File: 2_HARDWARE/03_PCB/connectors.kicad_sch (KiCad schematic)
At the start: 19 parts, among them J1 TYPE-C-31-M-12, J2 SMA, J3 SMA, J4 BNC, J5 PH-00244

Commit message: MINOR: Changed board outline and started component placement.
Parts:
- H1: footprint MountingHole:MountingHole_3.2mm_M3_Pad -> MountingHole:MountingHole_3.2mm_M3_Pad_TopBottom
- H2, H3, H4: footprint MountingHole:MountingHole_3.2mm_M3_Pad -> MountingHole:MountingHole_3.2mm_M3_Pad_Via
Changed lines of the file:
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@@
 			)
 		)
-		(property "Footprint" "MountingHole:MountingHole_3.2mm_M3_Pad"
+		(property "Footprint" "MountingHole:MountingHole_3.2mm_M3_Pad_Via"
 			(at 242.57 17.78 0)
 			(effects
@@
 	)
 	(symbol
+		(lib_name "MountingHole_Pad_1")
 		(lib_id "Mechanical:MountingHole_Pad")
 		(at 232.41 17.78 0)
@@
 			)
 		)
-		(property "Footprint" "MountingHole:MountingHole_3.2mm_M3_Pad"
+		(property "Footprint" "MountingHole:MountingHole_3.2mm_M3_Pad_TopBottom"
 			(at 232.41 17.78 0)
 			(effects
@@
 			)
 		)
-		(property "Footprint" "MountingHole:MountingHole_3.2mm_M3_Pad"
+		(property "Footprint" "MountingHole:MountingHole_3.2mm_M3_Pad_Via"
 			(at 251.46 17.78 0)
 			(effects
@@
 			)
 		)
-		(property "Footprint" "MountingHole:MountingHole_3.2mm_M3_Pad"
+		(property "Footprint" "MountingHole:MountingHole_3.2mm_M3_Pad_Via"
 			(at 260.35 17.78 0)
 			(effects

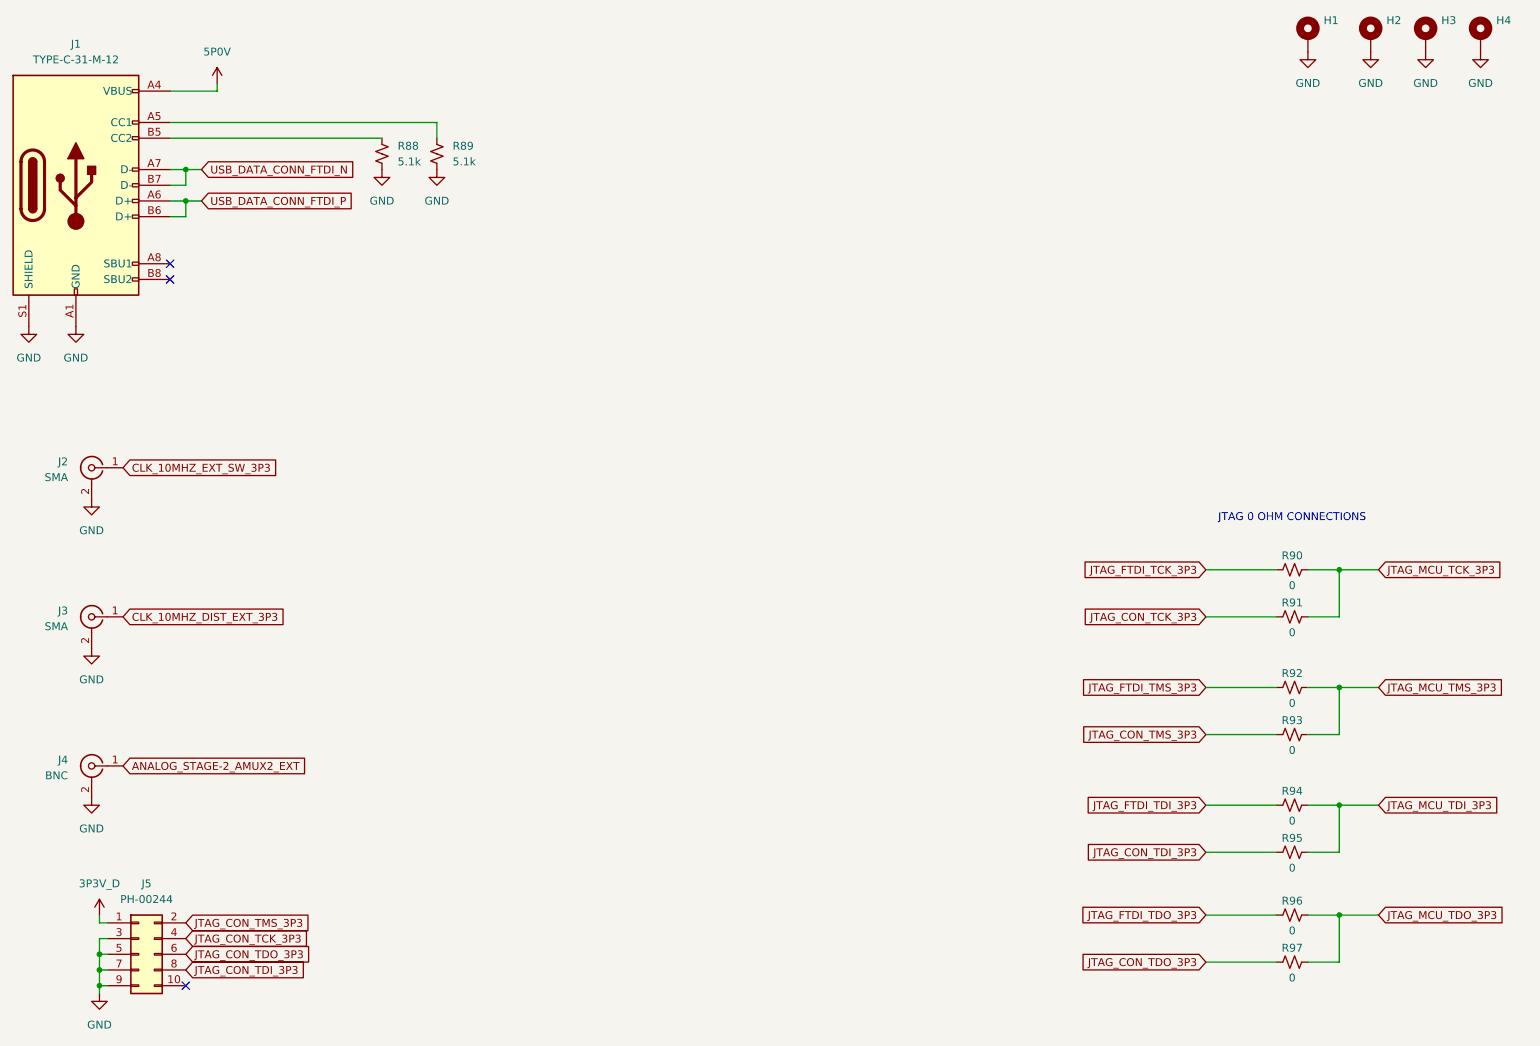
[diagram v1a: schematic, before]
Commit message: MINOR: Changed Boot Select Switches to Pull-Downs / Pull Up DNI and continued layout.
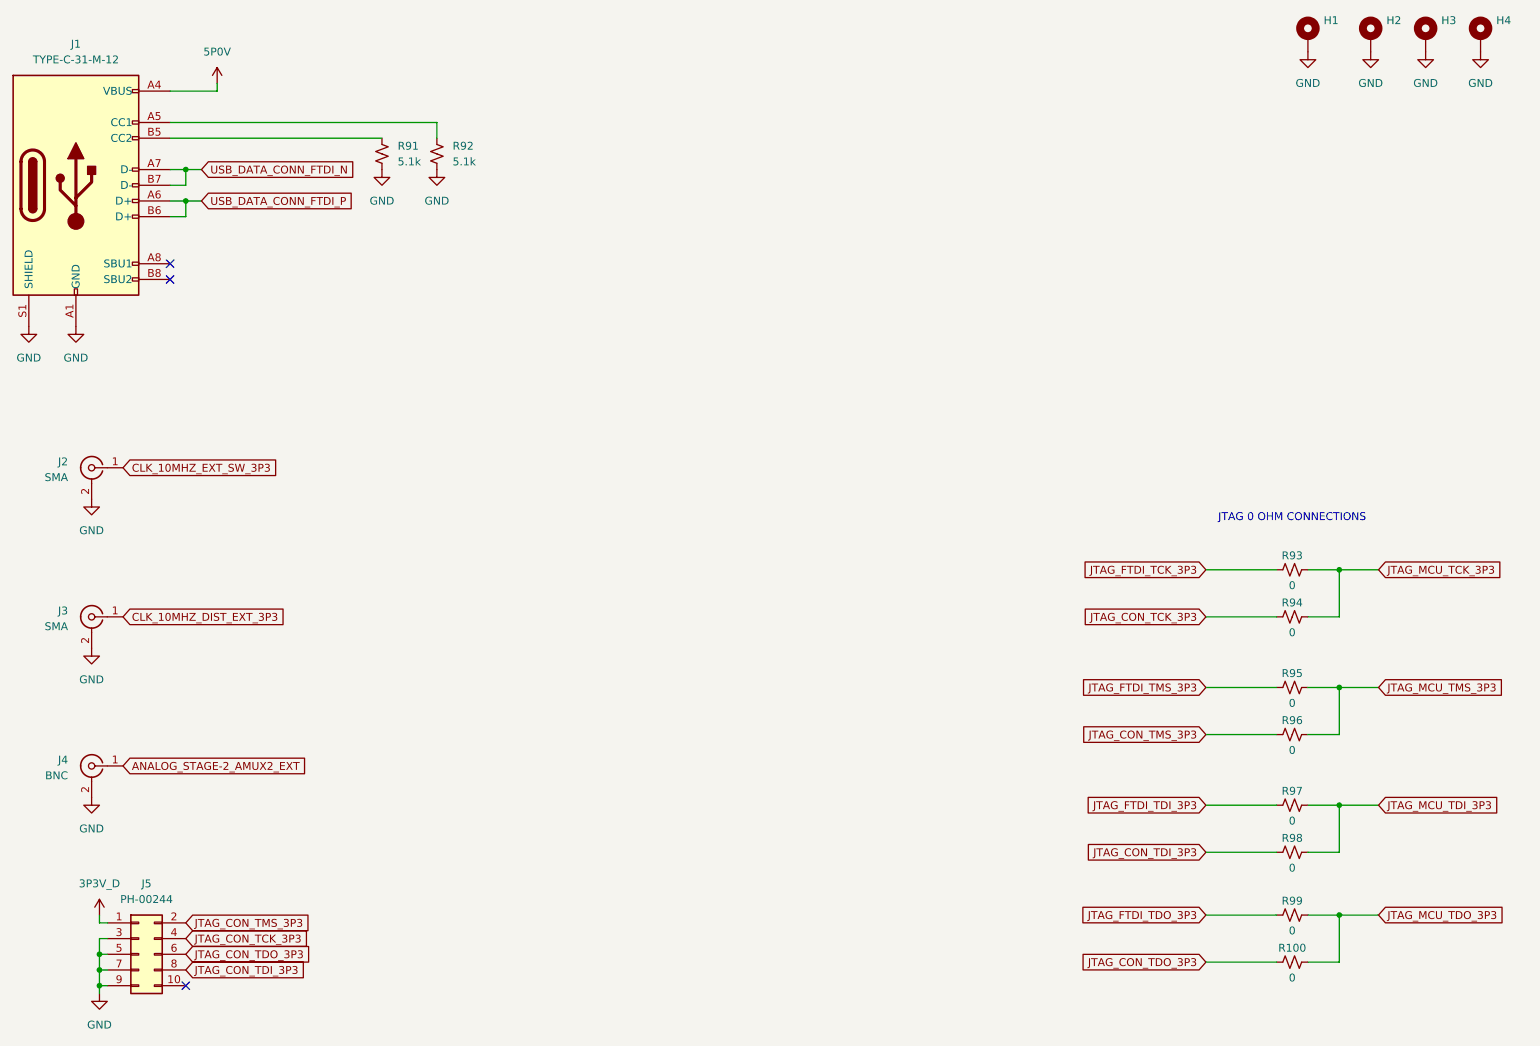
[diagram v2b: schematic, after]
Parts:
- renumbered R97 to R100, R88 to R91, R89 to R92, R90 to R93, R91 to R94, R92 to R95, R93 to R96, R94 to R97, R95 to R98, R96 to R99
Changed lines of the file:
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@@
 		(on_board yes)
 		(dnp no)
-		(property "Reference" "R97"
+		(property "Reference" "R100"
 			(at 229.87 165.354 90)
 			(effects
@@
 			(project "arb"
 				(path "/866ef9be-3b01-4288-a6e0-a2357aa17e50/eb105004-087f-4ea7-8291-809b214299af"
-					(reference "R97")
+					(reference "R100")
 					(unit 1)
 				)
@@
 		(dnp no)
 		(fields_autoplaced yes)
-		(property "Reference" "#PWR0299"
+		(property "Reference" "#PWR0295"
 			(at 35.56 147.32 0)
 			(effects
@@
 			(project "arb"
 				(path "/866ef9be-3b01-4288-a6e0-a2357aa17e50/eb105004-087f-4ea7-8291-809b214299af"
-					(reference "#PWR0299")
+					(reference "#PWR0295")
 					(unit 1)
 				)
@@
 		(dnp no)
 		(fields_autoplaced yes)
-		(property "Reference" "#PWR0300"
+		(property "Reference" "#PWR0296"
 			(at 36.83 163.83 0)
 			(effects
@@
 			(project "arb"
 				(path "/866ef9be-3b01-4288-a6e0-a2357aa17e50/eb105004-087f-4ea7-8291-809b214299af"
-					(reference "#PWR0300")
+					(reference "#PWR0296")
 					(unit 1)
 				)
@@
 		(on_board yes)
 		(dnp no)
-		(property "Reference" "R92"
+		(property "Reference" "R95"
 			(at 229.87 120.904 90)
 			(effects
@@
 			(project "arb"
 				(path "/866ef9be-3b01-4288-a6e0-a2357aa17e50/eb105004-087f-4ea7-8291-809b214299af"
-					(reference "R92")
+					(reference "R95")
 					(unit 1)
 				)
@@
 		(dnp no)
 		(fields_autoplaced yes)
-		(property "Reference" "#PWR0307"
+		(property "Reference" "#PWR0303"
 			(at 251.46 26.67 0)
 			(effects
@@
 			(project "arb"
 				(path "/866ef9be-3b01-4288-a6e0-a2357aa17e50/eb105004-087f-4ea7-8291-809b214299af"
-					(reference "#PWR0307")
+					(reference "#PWR0303")
 					(unit 1)
 				)
@@
 		(dnp no)
 		(fields_autoplaced yes)
-		(property "Reference" "R89"
+		(property "Reference" "R92"
 			(at 93.98 35.5599 0)
 			(effects
@@
 			(project "arb"
 				(path "/866ef9be-3b01-4288-a6e0-a2357aa17e50/eb105004-087f-4ea7-8291-809b214299af"
-					(reference "R89")
+					(reference "R92")
 					(unit 1)
 				)
@@
 		(dnp no)
 		(fields_autoplaced yes)
-		(property "Reference" "#PWR0295"
+		(property "Reference" "#PWR0291"
 			(at 25.4 71.12 0)
 			(effects
@@
 			(project "arb"
 				(path "/866ef9be-3b01-4288-a6e0-a2357aa17e50/eb105004-087f-4ea7-8291-809b214299af"
-					(reference "#PWR0295")
+					(reference "#PWR0291")
 					(unit 1)
 				)
@@
 		(dnp no)
 		(fields_autoplaced yes)
-		(property "Reference" "#PWR0303"
+		(property "Reference" "#PWR0299"
 			(at 82.55 45.72 0)
 			(effects
@@
 			(project "arb"
 				(path "/866ef9be-3b01-4288-a6e0-a2357aa17e50/eb105004-087f-4ea7-8291-809b214299af"
-					(reference "#PWR0303")
+					(reference "#PWR0299")
 					(unit 1)
 				)
@@
 		(dnp no)
 		(fields_autoplaced yes)
-		(property "Reference" "#PWR0297"
+		(property "Reference" "#PWR0293"
 			(at 35.56 99.06 0)
 			(effects
@@
 			(project "arb"
 				(path "/866ef9be-3b01-4288-a6e0-a2357aa17e50/eb105004-087f-4ea7-8291-809b214299af"
-					(reference "#PWR0297")
+					(reference "#PWR0293")
 					(unit 1)
 				)
@@
 		(dnp no)
 		(fields_autoplaced yes)
-		(property "Reference" "#PWR0298"
+		(property "Reference" "#PWR0294"
 			(at 35.56 123.19 0)
 			(effects
@@
 			(project "arb"
 				(path "/866ef9be-3b01-4288-a6e0-a2357aa17e50/eb105004-087f-4ea7-8291-809b214299af"
-					(reference "#PWR0298")
+					(reference "#PWR0294")
 					(unit 1)
 				)
@@
 		(dnp no)
 		(fields_autoplaced yes)
-		(property "Reference" "#PWR0308"
+		(property "Reference" "#PWR0304"
 			(at 260.35 26.67 0)
 			(effects
@@
 			(project "arb"
 				(path "/866ef9be-3b01-4288-a6e0-a2357aa17e50/eb105004-087f-4ea7-8291-809b214299af"
-					(reference "#PWR0308")
+					(reference "#PWR0304")
 					(unit 1)
 				)
@@
 		(dnp no)
 		(fields_autoplaced yes)
-		(property "Reference" "#PWR0306"
+		(property "Reference" "#PWR0302"
 			(at 242.57 26.67 0)
 			(effects
@@
 			(project "arb"
 				(path "/866ef9be-3b01-4288-a6e0-a2357aa17e50/eb105004-087f-4ea7-8291-809b214299af"
-					(reference "#PWR0306")
+					(reference "#PWR0302")
 					(unit 1)
 				)
@@
 		(dnp no)
 		(fields_autoplaced yes)
-		(property "Reference" "#PWR0301"
+		(property "Reference" "#PWR0297"
 			(at 36.83 179.07 0)
 			(effects
@@
 			(project "arb"
 				(path "/866ef9be-3b01-4288-a6e0-a2357aa17e50/eb105004-087f-4ea7-8291-809b214299af"
-					(reference "#PWR0301")
+					(reference "#PWR0297")
 					(unit 1)
 				)
@@
 		(dnp no)
 		(fields_autoplaced yes)
-		(property "Reference" "#PWR0304"
+		(property "Reference" "#PWR0300"
 			(at 91.44 45.72 0)
 			(effects
@@
 			(project "arb"
 				(path "/866ef9be-3b01-4288-a6e0-a2357aa17e50/eb105004-087f-4ea7-8291-809b214299af"
-					(reference "#PWR0304")
+					(reference "#PWR0300")
 					(unit 1)
 				)
@@
 		(on_board yes)
 		(dnp no)
-		(property "Reference" "R91"
+		(property "Reference" "R94"
 			(at 229.87 109.474 90)
 			(effects
@@
 			(project "arb"
 				(path "/866ef9be-3b01-4288-a6e0-a2357aa17e50/eb105004-087f-4ea7-8291-809b214299af"
-					(reference "R91")
+					(reference "R94")
 					(unit 1)
 				)
@@
 		(on_board yes)
 		(dnp no)
-		(property "Reference" "R94"
+		(property "Reference" "R97"
 			(at 229.87 139.954 90)
 			(effects
@@
 			(project "arb"
 				(path "/866ef9be-3b01-4288-a6e0-a2357aa17e50/eb105004-087f-4ea7-8291-809b214299af"
-					(reference "R94")
+					(reference "R97")
 					(unit 1)
 				)
@@
 		(dnp no)
 		(fields_autoplaced yes)
-		(property "Reference" "#PWR0296"
+		(property "Reference" "#PWR0292"
 			(at 33.02 71.12 0)
 			(effects
@@
 			(project "arb"
 				(path "/866ef9be-3b01-4288-a6e0-a2357aa17e50/eb105004-087f-4ea7-8291-809b214299af"
-					(reference "#PWR0296")
+					(reference "#PWR0292")
 					(unit 1)
 				)
@@
 		(on_board yes)
 		(dnp no)
-		(property "Reference" "R95"
+		(property "Reference" "R98"
 			(at 229.87 147.574 90)
 			(effects
@@
 			(project "arb"
 				(path "/866ef9be-3b01-4288-a6e0-a2357aa17e50/eb105004-087f-4ea7-8291-809b214299af"
-					(reference "R95")
+					(reference "R98")
 					(unit 1)
 				)
@@
 		(on_board yes)
 		(dnp no)
-		(property "Reference" "R96"
+		(property "Reference" "R99"
 			(at 229.87 157.734 90)
 			(effects
@@
 			(project "arb"
 				(path "/866ef9be-3b01-4288-a6e0-a2357aa17e50/eb105004-087f-4ea7-8291-809b214299af"
-					(reference "R96")
+					(reference "R99")
 					(unit 1)
 				)
@@
 		(on_board yes)
 		(dnp no)
-		(property "Reference" "R90"
+		(property "Reference" "R93"
 			(at 229.87 101.854 90)
 			(effects
@@
 			(project "arb"
 				(path "/866ef9be-3b01-4288-a6e0-a2357aa17e50/eb105004-087f-4ea7-8291-809b214299af"
-					(reference "R90")
+					(reference "R93")
 					(unit 1)
 				)
@@
 		(dnp no)
 		(fields_autoplaced yes)
-		(property "Reference" "#PWR0302"
+		(property "Reference" "#PWR0298"
 			(at 55.88 29.21 0)
 			(effects
@@
 			(project "arb"
 				(path "/866ef9be-3b01-4288-a6e0-a2357aa17e50/eb105004-087f-4ea7-8291-809b214299af"
-					(reference "#PWR0302")
+					(reference "#PWR0298")
 					(unit 1)
 				)
@@
 		(dnp no)
 		(fields_autoplaced yes)
-		(property "Reference" "R88"
+		(property "Reference" "R91"
 			(at 85.09 35.5599 0)
 			(effects
@@
 			(project "arb"
 				(path "/866ef9be-3b01-4288-a6e0-a2357aa17e50/eb105004-087f-4ea7-8291-809b214299af"
-					(reference "R88")
+					(reference "R91")
 					(unit 1)
 				)
@@
 		(dnp no)
 		(fields_autoplaced yes)
-		(property "Reference" "#PWR0305"
+		(property "Reference" "#PWR0301"
 			(at 232.41 26.67 0)
 			(effects
@@
 			(project "arb"
 				(path "/866ef9be-3b01-4288-a6e0-a2357aa17e50/eb105004-087f-4ea7-8291-809b214299af"
-					(reference "#PWR0305")
+					(reference "#PWR0301")
 					(unit 1)
 				)
@@
 		(on_board yes)
 		(dnp no)
-		(property "Reference" "R93"
+		(property "Reference" "R96"
 			(at 229.87 128.524 90)
 			(effects
@@
 			(project "arb"
 				(path "/866ef9be-3b01-4288-a6e0-a2357aa17e50/eb105004-087f-4ea7-8291-809b214299af"
-					(reference "R93")
-					(unit 1)
-				)
+					(reference "R96")
+					(unit 1)
+				)

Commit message: FEAT: Routed Analog and all Misc Signals. Routing is complete.
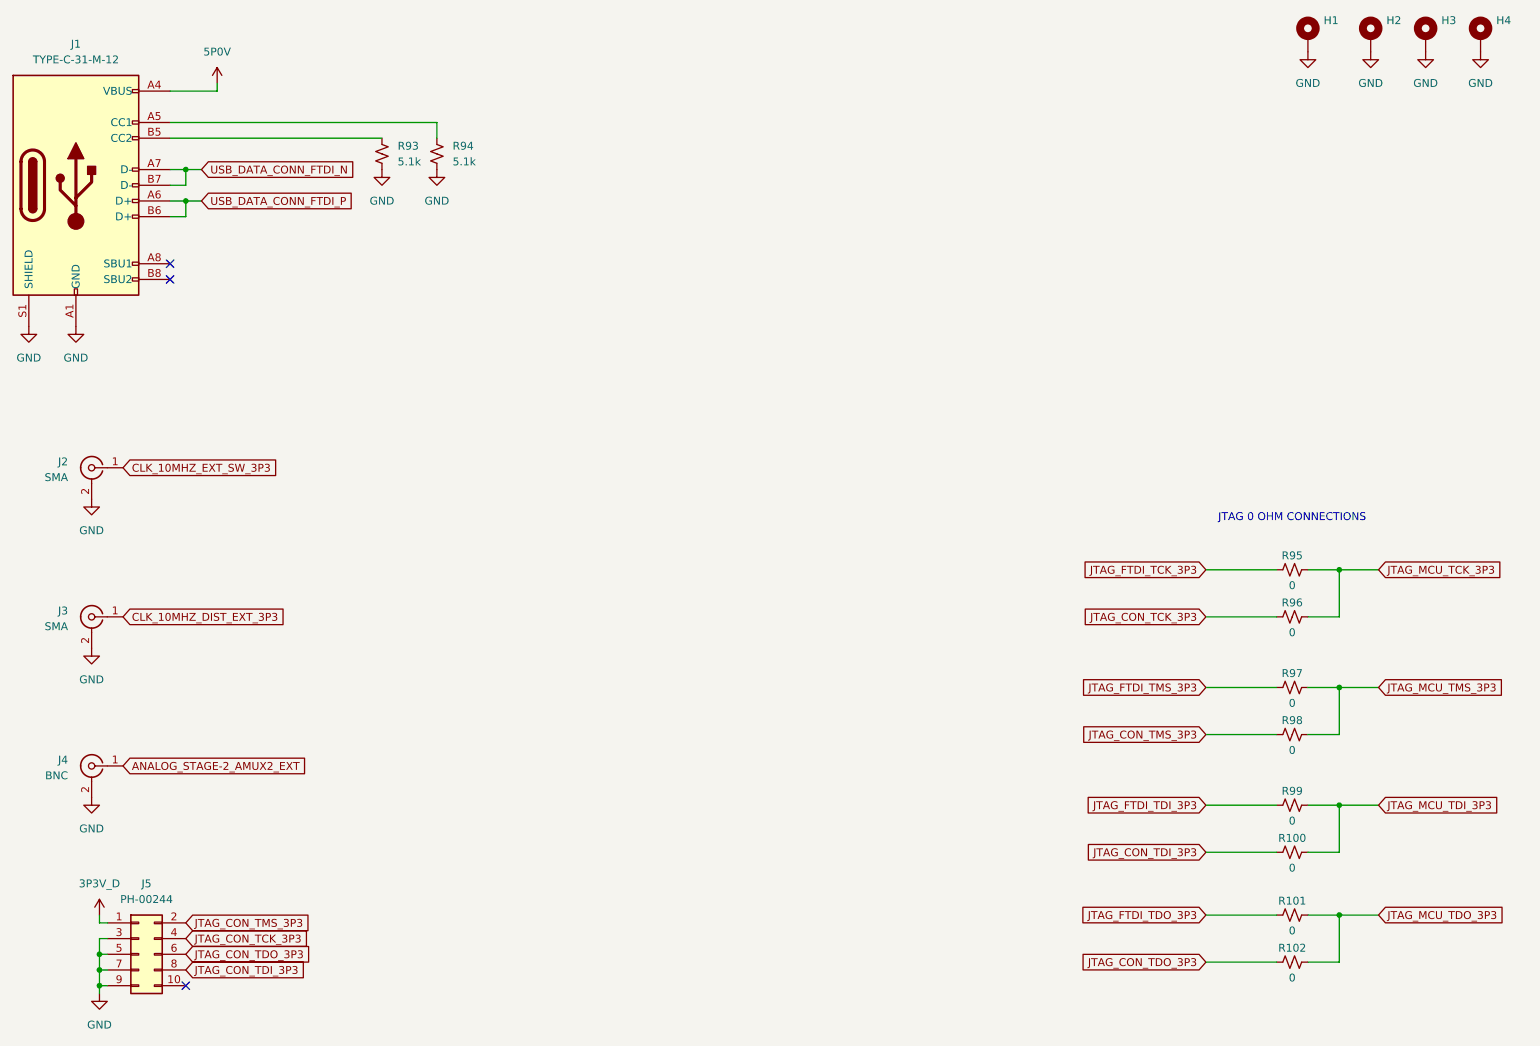
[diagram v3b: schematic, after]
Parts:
- renumbered R98 to R100, R99 to R101, R100 to R102, R91 to R93, R92 to R94, R93 to R95, R94 to R96, R95 to R97, R96 to R98, R97 to R99
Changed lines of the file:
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@@
 		(on_board yes)
 		(dnp no)
-		(property "Reference" "R100"
+		(property "Reference" "R102"
 			(at 229.87 165.354 90)
 			(effects
@@
 			(project "arb"
 				(path "/866ef9be-3b01-4288-a6e0-a2357aa17e50/eb105004-087f-4ea7-8291-809b214299af"
-					(reference "R100")
+					(reference "R102")
 					(unit 1)
 				)
@@
 		(on_board yes)
 		(dnp no)
-		(property "Reference" "R95"
+		(property "Reference" "R97"
 			(at 229.87 120.904 90)
 			(effects
@@
 			(project "arb"
 				(path "/866ef9be-3b01-4288-a6e0-a2357aa17e50/eb105004-087f-4ea7-8291-809b214299af"
-					(reference "R95")
+					(reference "R97")
 					(unit 1)
 				)
@@
 		(dnp no)
 		(fields_autoplaced yes)
-		(property "Reference" "R92"
+		(property "Reference" "R94"
 			(at 93.98 35.5599 0)
 			(effects
@@
 			(project "arb"
 				(path "/866ef9be-3b01-4288-a6e0-a2357aa17e50/eb105004-087f-4ea7-8291-809b214299af"
-					(reference "R92")
+					(reference "R94")
 					(unit 1)
 				)
@@
 		(on_board yes)
 		(dnp no)
-		(property "Reference" "R94"
+		(property "Reference" "R96"
 			(at 229.87 109.474 90)
 			(effects
@@
 			(project "arb"
 				(path "/866ef9be-3b01-4288-a6e0-a2357aa17e50/eb105004-087f-4ea7-8291-809b214299af"
-					(reference "R94")
+					(reference "R96")
 					(unit 1)
 				)
@@
 		(on_board yes)
 		(dnp no)
-		(property "Reference" "R97"
+		(property "Reference" "R99"
 			(at 229.87 139.954 90)
 			(effects
@@
 			(project "arb"
 				(path "/866ef9be-3b01-4288-a6e0-a2357aa17e50/eb105004-087f-4ea7-8291-809b214299af"
-					(reference "R97")
+					(reference "R99")
 					(unit 1)
 				)
@@
 		(on_board yes)
 		(dnp no)
-		(property "Reference" "R98"
+		(property "Reference" "R100"
 			(at 229.87 147.574 90)
 			(effects
@@
 			(project "arb"
 				(path "/866ef9be-3b01-4288-a6e0-a2357aa17e50/eb105004-087f-4ea7-8291-809b214299af"
-					(reference "R98")
+					(reference "R100")
 					(unit 1)
 				)
@@
 		(on_board yes)
 		(dnp no)
-		(property "Reference" "R99"
+		(property "Reference" "R101"
 			(at 229.87 157.734 90)
 			(effects
@@
 			(project "arb"
 				(path "/866ef9be-3b01-4288-a6e0-a2357aa17e50/eb105004-087f-4ea7-8291-809b214299af"
-					(reference "R99")
+					(reference "R101")
 					(unit 1)
 				)
@@
 		(on_board yes)
 		(dnp no)
-		(property "Reference" "R93"
+		(property "Reference" "R95"
 			(at 229.87 101.854 90)
 			(effects
@@
 			(project "arb"
 				(path "/866ef9be-3b01-4288-a6e0-a2357aa17e50/eb105004-087f-4ea7-8291-809b214299af"
-					(reference "R93")
+					(reference "R95")
 					(unit 1)
 				)
@@
 		(dnp no)
 		(fields_autoplaced yes)
-		(property "Reference" "R91"
+		(property "Reference" "R93"
 			(at 85.09 35.5599 0)
 			(effects
@@
 			(project "arb"
 				(path "/866ef9be-3b01-4288-a6e0-a2357aa17e50/eb105004-087f-4ea7-8291-809b214299af"
-					(reference "R91")
+					(reference "R93")
 					(unit 1)
 				)
@@
 		(on_board yes)
 		(dnp no)
-		(property "Reference" "R96"
+		(property "Reference" "R98"
 			(at 229.87 128.524 90)
 			(effects
@@
 			(project "arb"
 				(path "/866ef9be-3b01-4288-a6e0-a2357aa17e50/eb105004-087f-4ea7-8291-809b214299af"
-					(reference "R96")
-					(unit 1)
-				)
+					(reference "R98")
+					(unit 1)
+				)
